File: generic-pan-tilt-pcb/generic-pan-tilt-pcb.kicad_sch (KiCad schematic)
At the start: 35 parts, among them J1 B4PS-VH, J10 USB4105-GF-A, J2 NC5MAV, J3 NC5FAV, J4 Conn_01x03, J5 BM03B-SRSS-TB, J6 Conn_01x03, J7 BM03B-SRSS-TB, J8 B12B-PH-SM4-TB, J9 B12B-PH-SM4-TB, SW1 PTS 647 SK70 SMTR2 LFS, SW2 PTS 647 SK70 SMTR2 LFS

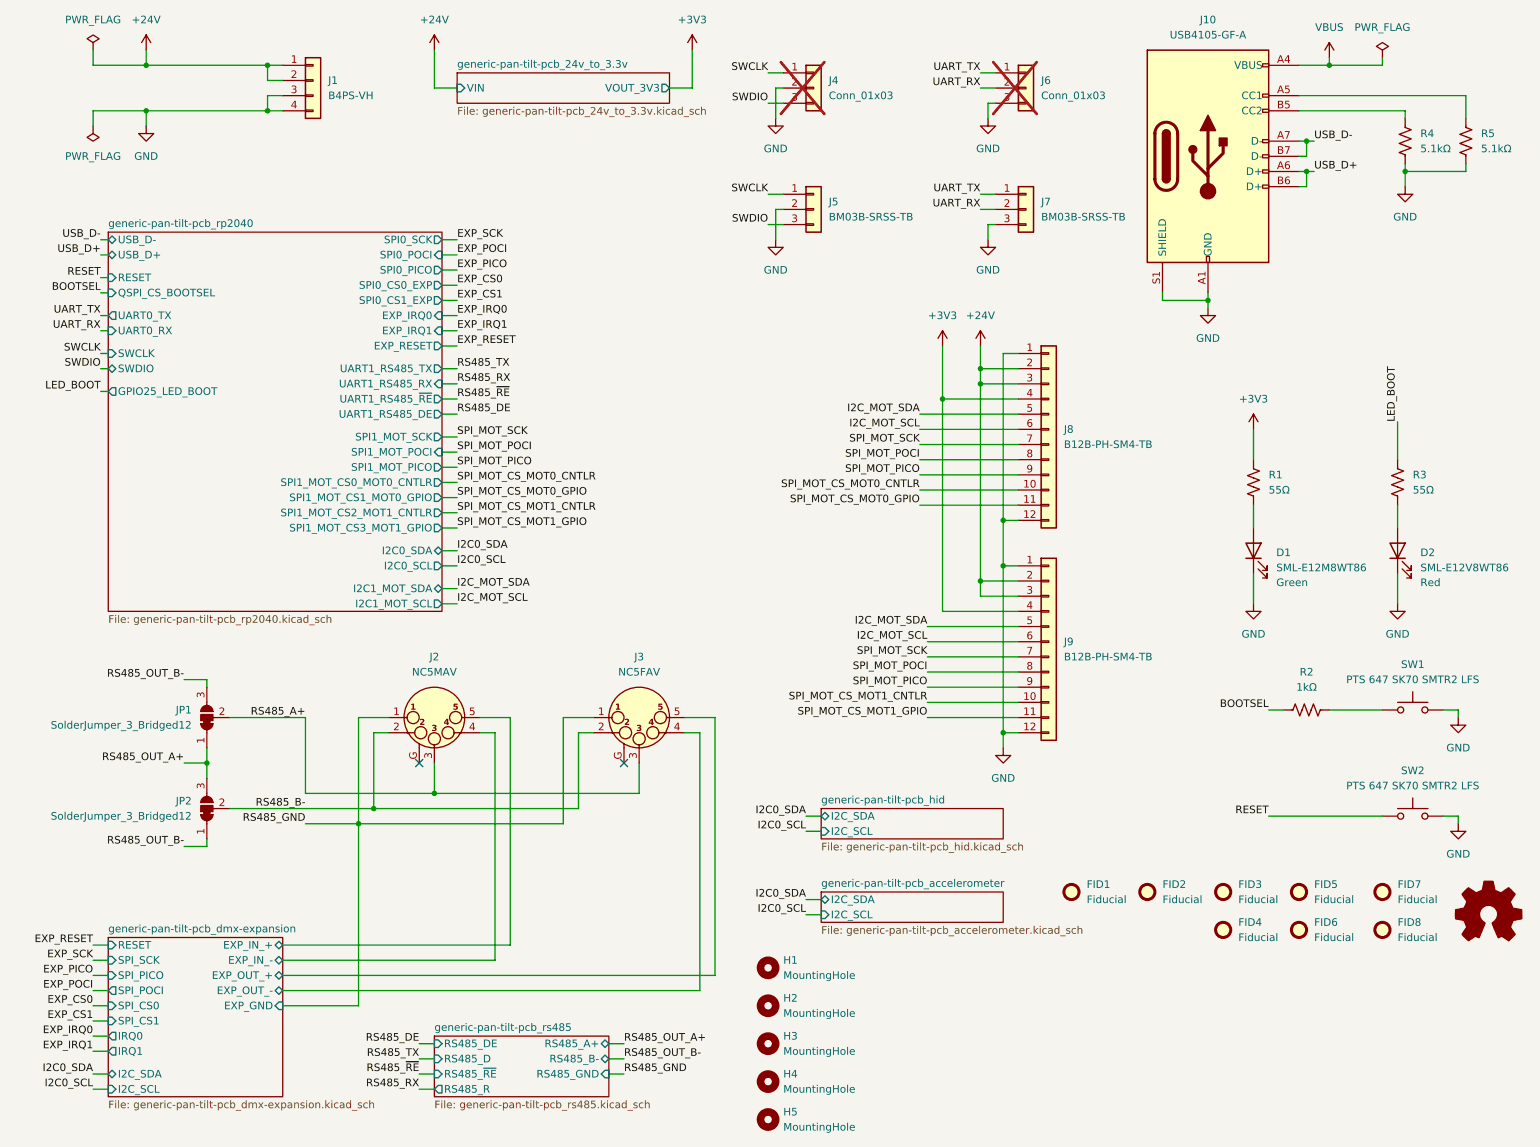
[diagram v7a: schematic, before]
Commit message: main board fix usb, fix uart, all caps and resistors manf and vendor, sch only replace psu and accel caps
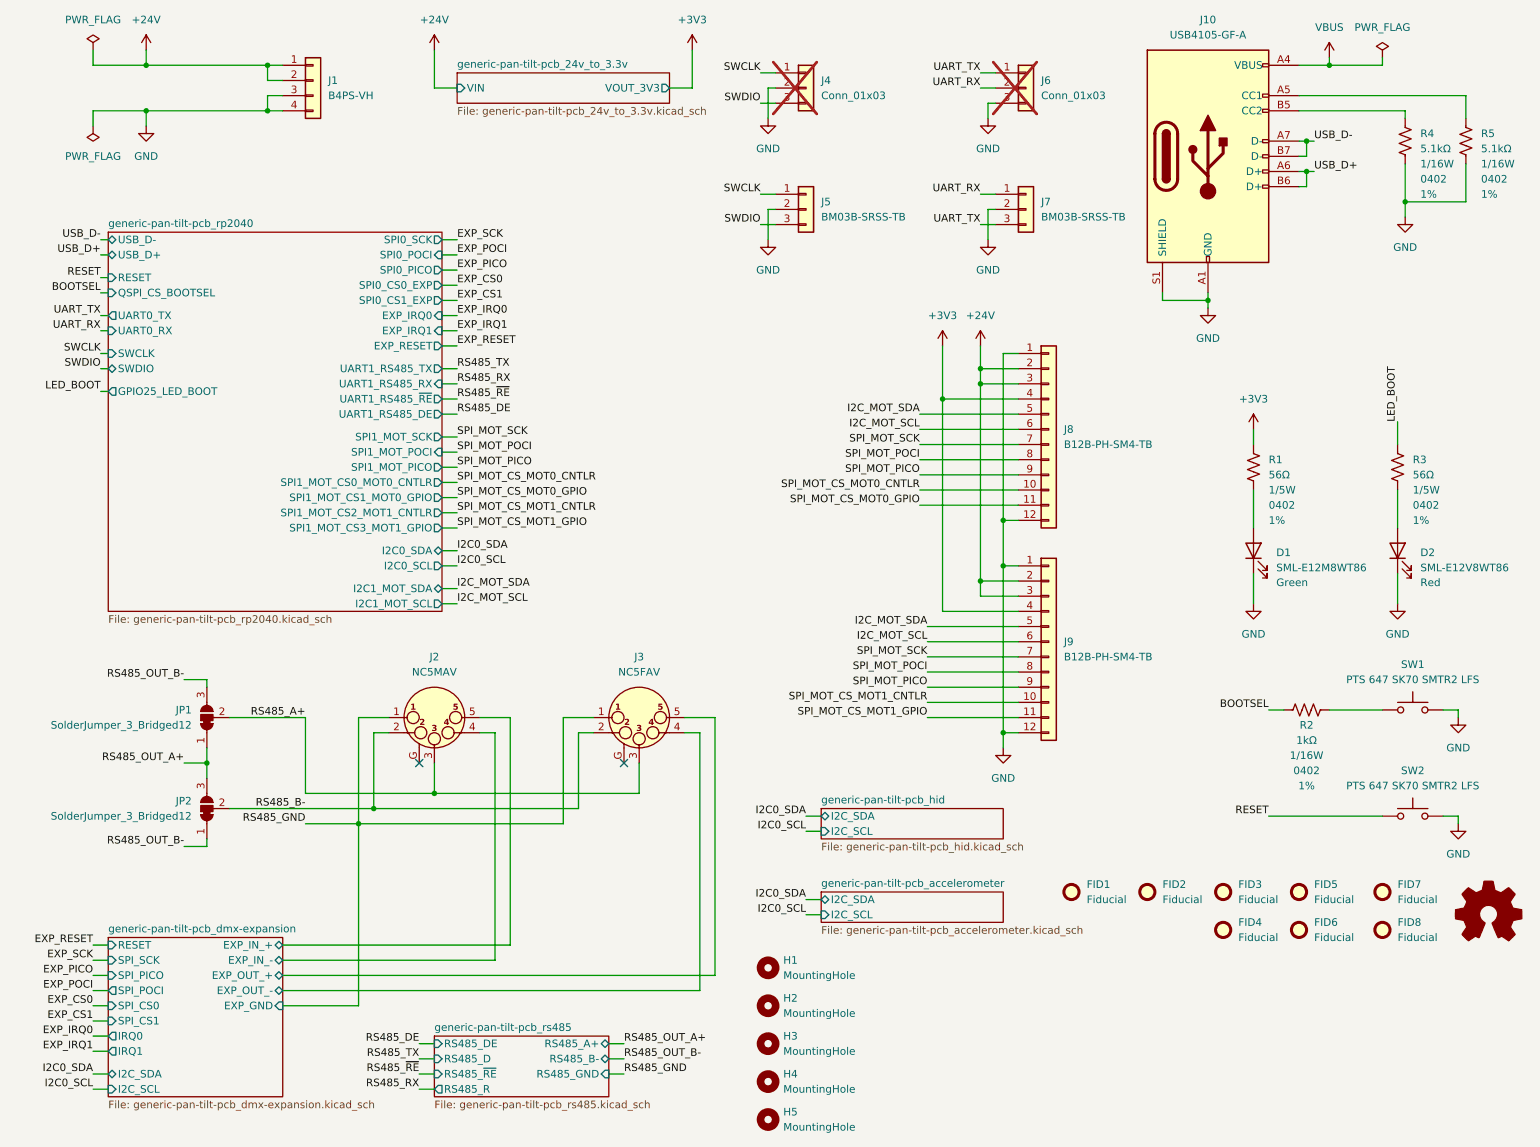
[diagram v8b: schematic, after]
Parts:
- D1: lcsc# (none) -> C2837819
- D2: lcsc# (none) -> C510294
- J1: lcsc# (none) -> C157996
- J10: lcsc# (none) -> C3020560
- J2: lcsc# (none) -> C368510
- J3: lcsc# (none) -> C368512
- J5, J7: lcsc# (none) -> C160389
- J8, J9: lcsc# (none) -> C545752
- R1, R3: value 55Ω -> 56Ω; Case Code (none) -> 0402; Power (none) -> 1/5W; Tolerance (none) -> 1%; digikey# (none) -> 541-10417-1-ND; lcsc# (none) -> C4063621; manf# (none) -> RCS040256R0FKED; mouser# (none) -> 71-RCS040256R0FKED
- R2: Case Code (none) -> 0402; Power (none) -> 1/16W; Tolerance (none) -> 1%; digikey# (none) -> CR0402-FX-1001GLFCT-ND; lcsc# (none) -> C202394; manf# (none) -> CR0402-FX-1001GLF; mouser# (none) -> 652-CR0402FX-1001GLF; newark# (none) -> 02J1761
- R4, R5: Case Code (none) -> 0402; Power (none) -> 1/16W; Tolerance (none) -> 1%; digikey# (none) -> CR0402-FX-5101GLFCT-ND; lcsc# (none) -> C19946460; manf# (none) -> CR0402-FX-5101GLF; mouser# (none) -> 652-CR0402FX-5101GLF; newark# (none) -> 33AK7356
- SW1, SW2: lcsc# (none) -> C2800043
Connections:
- net GND: now also J7.2 (Pin_2), R4.1; no longer J7.3 (Pin_3), R4.2
- net UART_RX: now also J7.1 (Pin_1); no longer J7.2 (Pin_2)
- net UART_TX: now also J7.3 (Pin_3); no longer J7.1 (Pin_1)
- net at J10.B5 (CC2): now also R4.2; no longer R4.1
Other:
- moved on the sheet: J4
